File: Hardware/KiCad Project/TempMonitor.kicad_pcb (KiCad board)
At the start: 2 copper layers, 50 x 100 mm, 38 parts, among them M1 SMD-RES-10K-1%-1_8W_0805_, M2 SMD-RES-10K-1%-1_8W_0805_, M3 SMD-RES-10K-1%-1_8W_0805_, M4 SMD-RES-10K-1%-1_8W_0805_, M5 SMD-RES-10K-1%-1_8W_0805_, M6 SMD-RES-10K-1%-1_8W_0805_, M7 SMD-RES-10K-1%-1_8W_0805_, M8 SMD-RES-10K-1%-1_8W_0805_, M9 SMD-RES-10K-1%-1_8W_0805_, P1 Pad, P10 Pad, P11 Pad, P2 ProgrammingPad, P3 Pad, P4 Pad, P5 Pad, P6 Pad, P7 Pad, P8 Pad, P9 Pad, U1 DRIVER-TM1637_SOP20_, U2 LED-4-BETY-7-SEG_2X7P-30X14MM_, U3 LED-4-BETY-7-SEG_2X7P-30X14MM_, U4 LED-4-BETY-7-SEG_2X7P-30X14MM_, U5 LED-4-BETY-7-SEG_2X7P-30X14MM_, U6 DRIVER-TM1637_SOP20_, U7 DRIVER-TM1637_SOP20_, U8 DRIVER-TM1637_SOP20_, U9 ATMEGA16U2-MU, Y1 SMD-CRYSTAL-16MHZ-8PF-20PPM-4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

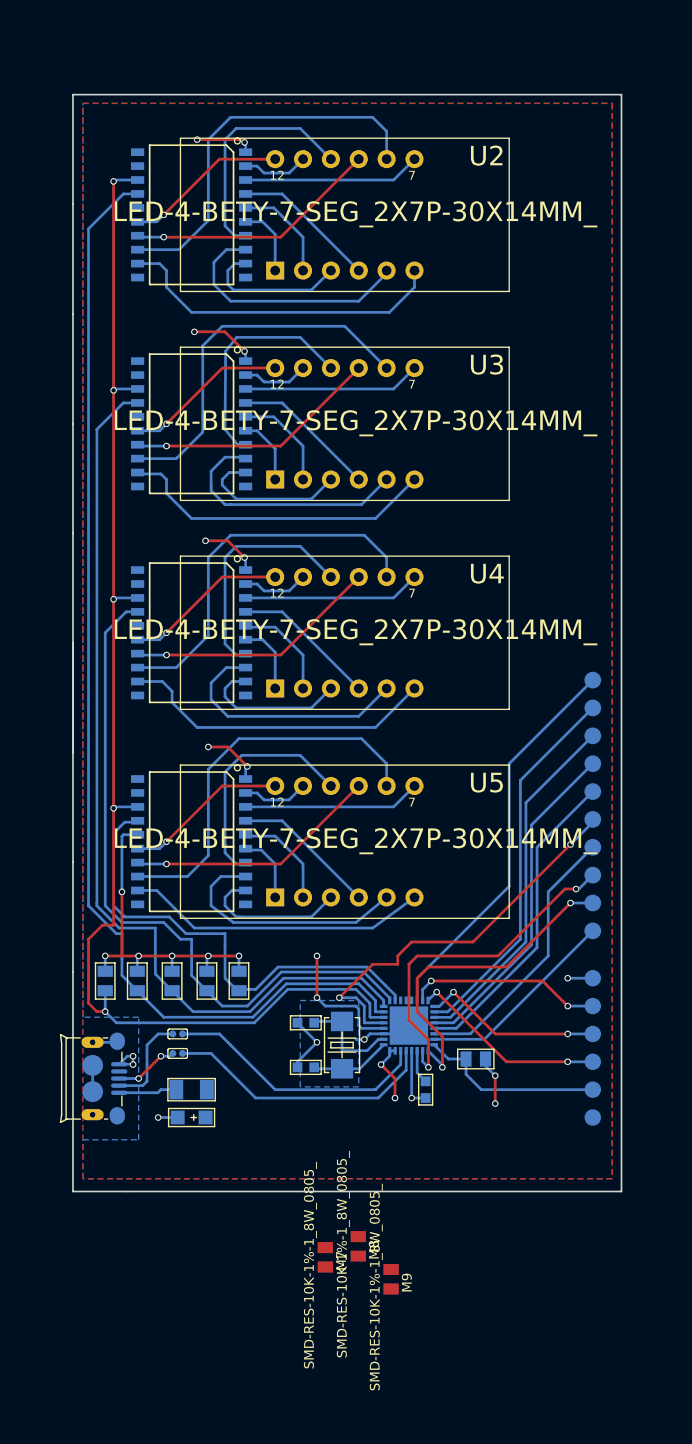
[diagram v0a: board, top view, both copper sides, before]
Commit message: Update
Gerber files added, BOM added, PCB redone, separate clock traces for
led-drivers made.
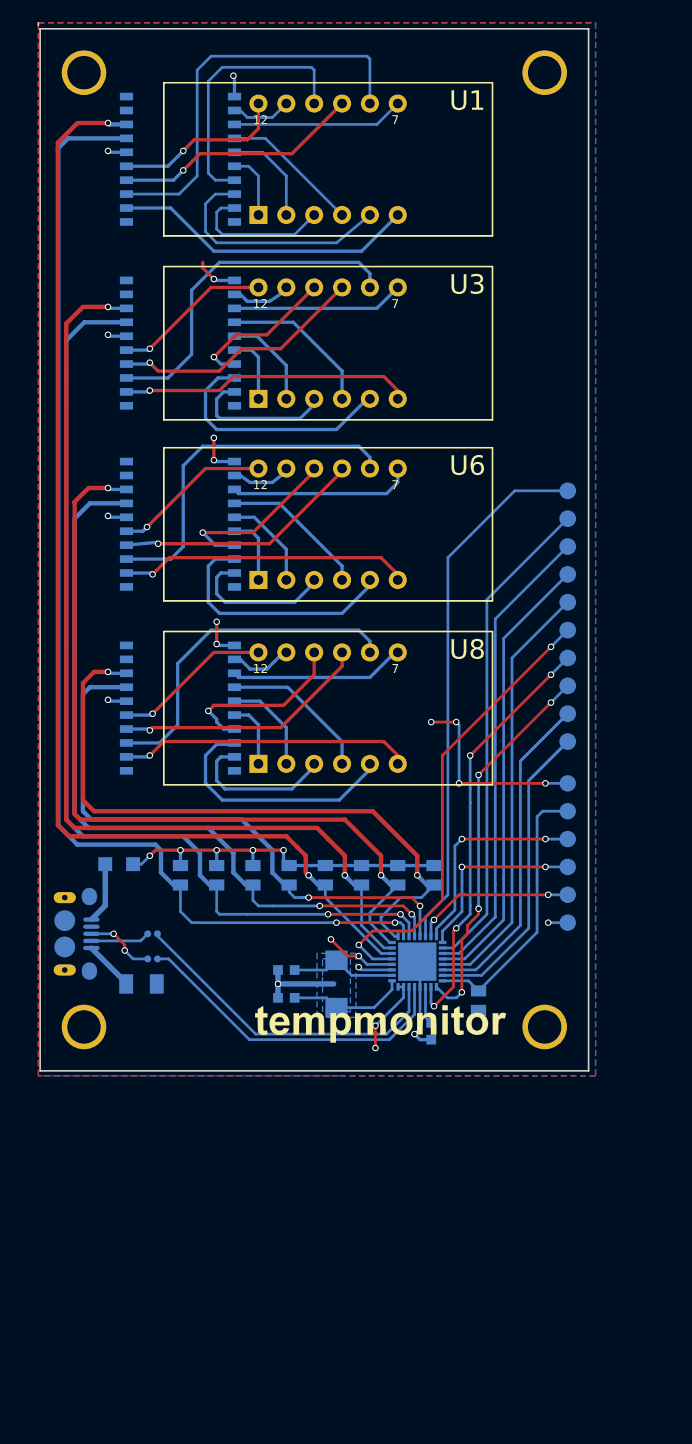
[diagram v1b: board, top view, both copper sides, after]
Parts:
- removed M1, M2, M3, M4, M5, M6: SMD-RES-10K-1%-1_8W_0805_, R0805
- removed M7, M8, M9: SMD-RES-10K-1%-1_8W_0805_, Seeed-Resistor-2016:R0805
- added G***: LOGO, Homebrew:LOGO, F.Cu at (148.6, 134.4)
- added R10: SMD-RES-10K-1%-1_8W_0805_, Seeed-Resistor-2016:R0805, B.Cu at (157.0, 132.6)
- added R11: SMD-RES-22R-1%-1_16W_0402_, Seeed-Resistor-2016:R0402, B.Cu at (127.3, 128.8)
- added R3: SMD-RES-10K-1%-1_8W_0805_, Seeed-Resistor-2016:R0805, B.Cu at (149.6, 121.2)
- added R4: SMD-RES-10K-1%-1_8W_0805_, Seeed-Resistor-2016:R0805, B.Cu at (152.9, 121.2)
- added R5: SMD-RES-10K-1%-1_8W_0805_, Seeed-Resistor-2016:R0805, B.Cu at (129.8, 121.2)
- added R6: SMD-RES-10K-1%-1_8W_0805_, Seeed-Resistor-2016:R0805, B.Cu at (133.1, 121.2)
- added R7: SMD-RES-10K-1%-1_8W_0805_, Seeed-Resistor-2016:R0805, B.Cu at (136.4, 121.2)
- added R8: SMD-RES-10K-1%-1_8W_0805_, Seeed-Resistor-2016:R0805, B.Cu at (139.7, 121.2)
- added R9: SMD-RES-22R-1%-1_16W_0402_, Seeed-Resistor-2016:R0402, B.Cu at (127.3, 126.5)
- added REF**: 1pin, Connect:1pin, F.Cu at (163.0, 135.0)
- added REF**: 1pin, Connect:1pin, F.Cu at (163.0, 48.0)
- added REF**: 1pin, Connect:1pin, F.Cu at (121.0, 48.0)
- added REF**: 1pin, Connect:1pin, F.Cu at (121.0, 135.0)
- C1: footprint AVX-A -> Seeed-Capacitor-2016:AVX-A
- C2: value CERAMIC-10PF-50V-5%-NPO_0603_ -> CERAMIC-1UF-25V-10%-X7R_0603_; footprint C0603 -> Seeed-Capacitor-2016:C0603
- C3: footprint C0603 -> Seeed-Capacitor-2016:C0603
- C4: value CERAMIC-1UF-25V-10%-X7R_0603_ -> CERAMIC-10PF-50V-5%-NPO_0603_; footprint C0603 -> Seeed-Capacitor-2016:C0603
- F1: footprint F1206 -> Seeed-Fuse-2016:F1206
- P1, P10, P3, P4, P5, P6, P7, P8, P9: moved to B.Cu
- P11: value Pad -> ProgrammingPad; footprint Homebrew:Pad -> Homebrew:ProgrammingPad
- P2: value ProgrammingPad -> Pad; footprint Homebrew:ProgrammingPad -> Homebrew:Pad; moved to B.Cu
- R1, R2: value SMD-RES-22R-1%-1_16W_0402_ -> SMD-RES-10K-1%-1_8W_0805_; footprint R0402 -> Seeed-Resistor-2016:R0805
- U1: value DRIVER-TM1637_SOP20_ -> LED-4-BETY-7-SEG_2X7P-30X14MM_; footprint SOP20-1.27-12.7X7.65MM -> Seeed-Display-2016:LCD12-2.54-30.0X14.0X7.3MM; moved to F.Cu
- U2, U4: value LED-4-BETY-7-SEG_2X7P-30X14MM_ -> DRIVER-TM1637_SOP20_; footprint LCD12-2.54-30.0X14.0X7.3MM -> Seeed-IC-2016:SOP20-1.27-12.7X7.65MM; moved to B.Cu
- U3: footprint LCD12-2.54-30.0X14.0X7.3MM -> Seeed-Display-2016:LCD12-2.54-30.0X14.0X7.3MM
- U5: value LED-4-BETY-7-SEG_2X7P-30X14MM_ -> ATMEGA16U2-MU; footprint LCD12-2.54-30.0X14.0X7.3MM -> ATMEGA16U2-MU:QFN50P500X500X100-33N; moved to B.Cu
- U6, U8: value DRIVER-TM1637_SOP20_ -> LED-4-BETY-7-SEG_2X7P-30X14MM_; footprint Seeed-IC-2016:SOP20-1.27-12.7X7.65MM -> Seeed-Display-2016:LCD12-2.54-30.0X14.0X7.3MM; moved to F.Cu
- U9: value ATMEGA16U2-MU -> DRIVER-TM1637_SOP20_; footprint ATMEGA16U2-MU:QFN50P500X500X100-33N -> Seeed-IC-2016:SOP20-1.27-12.7X7.65MM
- USB1: footprint MICRO-USB5+6P-SMD-0.65-B -> Homebrew:MICRO-USB5+6P-SMD-0.65-B_NY
- Y1: footprint X2-SMD-5.0X3.2X1.3MM -> Seeed-Crystal Oscillator-2016:X2-SMD-5.0X3.2X1.3MM
- moved P2 47.0 mm to (165.1, 88.7), turned to 0 degrees
- moved U9 35.7 mm to (129.8, 105.9), turned to 270 degrees
- moved U4 30.4 mm to (129.8, 72.7), turned to 270 degrees
- moved C1 24.0 mm to (124.2, 120.2)
- moved R2 22.1 mm to (146.3, 121.2), turned to 0 degrees
- moved R1 21.1 mm to (143.0, 121.2), turned to 0 degrees
- moved P10 19.9 mm to (165.1, 106.4), turned to 0 degrees
- moved U8 17.4 mm to (143.3, 105.9), turned to 0 degrees
- moved P4 17.4 mm to (165.1, 93.7), turned to 0 degrees
- moved P1 17.4 mm to (165.1, 86.1), turned to 0 degrees
- moved P8 17.4 mm to (165.1, 103.9), turned to 0 degrees
- moved C4 16.7 mm to (139.4, 129.8), turned to 270 degrees
- moved U2 15.8 mm to (129.8, 55.9), turned to 270 degrees
- moved U6 15.5 mm to (143.3, 89.2), turned to 0 degrees
- moved P3 14.9 mm to (165.1, 91.2), turned to 0 degrees
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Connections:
- C2 pad 1: GND -> Net-(C2-Pad1)
- C2 pad 2: Net-(C2-Pad2) -> GND
- C4 pad 1: Net-(C4-Pad1) -> GND
- C4 pad 2: GND -> Net-(C4-Pad2)
- P11 pad 1: Net-(P11-Pad1) -> VCC
- P2 pad 1: VCC -> Net-(P2-Pad1)
- R1 pad 1: D+ -> CLK1
- R1 pad 2: Net-(R1-Pad2) -> VCC
- R2 pad 1: D- -> CLK2
- R2 pad 2: Net-(R2-Pad2) -> VCC
- U1 pad 1: GND -> E1
- U1 pad 10: Net-(U1-Pad10) -> F1
- U1 pad 11: Net-(U1-Pad11) -> A1
- U1 pad 12: GR41 -> GR11
- U1 pad 2: A1 -> D1
- U1 pad 3: B1 -> DP1
- U1 pad 5: D1 -> G1
- U1 pad 6: E1 -> GR41
- U1 pad 7: F1 -> B1
- U1 pad 8: G1 -> GR31
- U1 pad 9: DP1 -> GR21
- U2 pad 1: E1 -> GND
- U2 pad 10: F1 -> Net-(U2-Pad10)
- U2 pad 11: A1 -> Net-(U2-Pad11)
- U2 pad 12: GR11 -> GR41
- U2 pad 2: D1 -> A1
- U2 pad 3: DP1 -> B1
- U2 pad 5: G1 -> D1
- U2 pad 6: GR41 -> E1
- U2 pad 7: B1 -> F1
- U2 pad 8: GR31 -> G1
- U2 pad 9: GR21 -> DP1
- U4 pad 1: E3 -> GND
- U4 pad 10: F3 -> Net-(U4-Pad10)
- U4 pad 11: A3 -> Net-(U4-Pad11)
- U4 pad 12: GR13 -> GR42
- U4 pad 2: D3 -> A2
- U4 pad 3: DP3 -> B2
- U4 pad 4: C3 -> C2
- U4 pad 5: G3 -> D2
- U4 pad 6: GR43 -> E2
- U4 pad 7: B3 -> F2
- U4 pad 8: GR33 -> G2
- U4 pad 9: GR23 -> DP2
- U5 pad 1: E4 -> Net-(C3-Pad2)
- U5 pad 10: F4 -> DATA1
- U5 pad 11: A4 -> DATA2
- U5 pad 12: GR14 -> DATA3
- U5 pad 2: D4 -> Net-(C4-Pad2)
- U5 pad 3: DP4 -> GND
- U5 pad 4: C4 -> VCC
- U5 pad 5: G4 -> Net-(P6-Pad1)
- U5 pad 6: GR44 -> CLK1
- U5 pad 7: B4 -> CLK2
- U5 pad 8: GR34 -> CLK3
- U5 pad 9: GR24 -> CLK4
- U6 pad 1: GND -> E3
- U6 pad 10: Net-(U6-Pad10) -> F3
- U6 pad 11: Net-(U6-Pad11) -> A3
- U6 pad 12: GR42 -> GR13
- U6 pad 2: A2 -> D3
- U6 pad 3: B2 -> DP3
- U6 pad 4: C2 -> C3
- U6 pad 5: D2 -> G3
- U6 pad 6: E2 -> GR43
- U6 pad 7: F2 -> B3
- U6 pad 8: G2 -> GR33
- U6 pad 9: DP2 -> GR23
- U7 pad 18: CLK -> CLK3
- U8 pad 1: GND -> E4
- U8 pad 10: Net-(U8-Pad10) -> F4
- U8 pad 11: Net-(U8-Pad11) -> A4
- U8 pad 12: GR44 -> GR14
- U8 pad 2: A4 -> D4
- U8 pad 3: B4 -> DP4
- U8 pad 5: D4 -> G4
- U8 pad 6: E4 -> GR44
- U8 pad 7: F4 -> B4
- U8 pad 8: G4 -> GR34
- U8 pad 9: DP4 -> GR24
- U9 pad 1: Net-(C2-Pad2) -> GND
- U9 pad 10: DATA1 -> Net-(U9-Pad10)
- U9 pad 11: DATA2 -> Net-(U9-Pad11)
- U9 pad 12: DATA3 -> GR44
- U9 pad 13: DATA4 -> GR34
- U9 pad 14: Net-(P1-Pad1) -> GR24
- U9 pad 15: SCK -> GR14
- U9 pad 16: MOSI -> VCC
- U9 pad 17: MISO -> DATA4
- U9 pad 18: Net-(P3-Pad1) -> CLK4
- U9 pad 19: Net-(P5-Pad1) -> Net-(U9-Pad19)
- U9 pad 2: Net-(C3-Pad2) -> A4
- U9 pad 20: Net-(P4-Pad1) -> Net-(U9-Pad20)
- U9 pad 3: GND -> B4
- U9 pad 4: VCC -> C4
- U9 pad 5: Net-(P7-Pad1) -> D4
- U9 pad 6: CLK1 -> E4
- U9 pad 7: CLK2 -> F4
- U9 pad 8: CLK3 -> G4
- U9 pad 9: CLK4 -> DP4
- Y1 pad 1: Net-(C2-Pad2) -> Net-(C3-Pad2)
- Y1 pad 2: Net-(C3-Pad2) -> Net-(C4-Pad2)
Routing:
- net CLK: track 87.3 -> 0.00 mm, vias 4 -> 0
- net CLK1: track 30.8 -> 106.4 mm, vias 1 -> 2
- net DATA1: track 106.2 -> 169.3 mm, vias 0 -> 2
- net CLK2: track 30.4 -> 89.1 mm, vias 0 -> 2
- net CLK3: track 29.2 -> 74.2 mm, vias 0 -> 2
- net Net-(P2-Pad1): track 0.00 -> 44.4 mm
- net DATA4: track 10.7 -> 54.3 mm, vias 0 -> 2
- net DATA2: track 54.3 -> 88.9 mm, vias 0 -> 2
- net CLK4: track 26.0 -> 60.0 mm, vias 0 -> 2
- net DATA3: track 36.9 -> 70.7 mm, vias 0 -> 2
- net Net-(R11-Pad2): track 0.00 -> 30.0 mm
- net Net-(R9-Pad2): track 0.00 -> 29.9 mm
- net Net-(P11-Pad1): track 24.9 -> 0.00 mm
- net Net-(R1-Pad2): track 24.9 -> 0.00 mm
- net Net-(R2-Pad2): track 24.2 -> 0.00 mm
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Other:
- board size 50 x 100 mm -> 50.2 x 95.6 mm

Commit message: Update
Logo exchanged, gerbers updated and BOM updated and redone, now with MPN
instead of Seeed SKU.
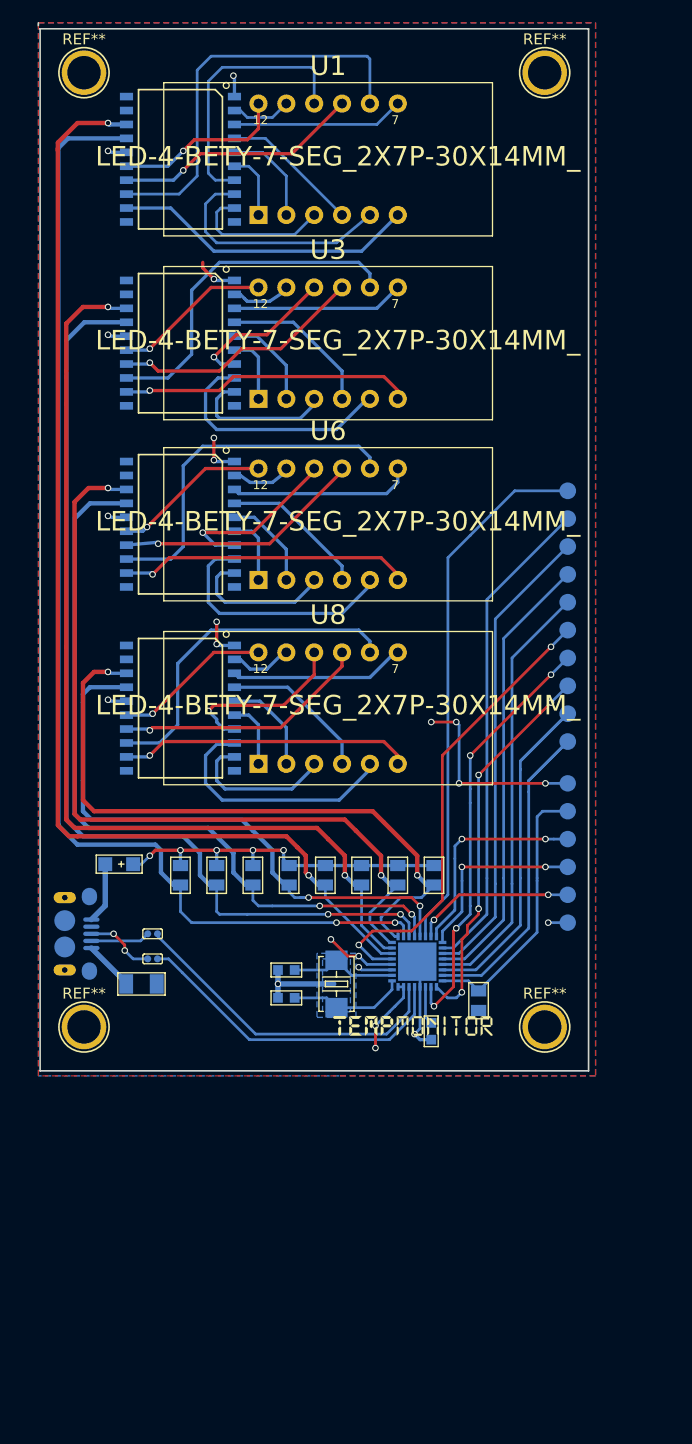
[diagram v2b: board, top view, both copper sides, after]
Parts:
- moved G*** 2.37 mm to (150.9, 134.7)
